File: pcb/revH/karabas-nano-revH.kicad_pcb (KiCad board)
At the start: 2 copper layers, 99.6 x 99.6 mm, 161 parts, among them J1 USB_B_Micro, J10 PWR, J11 AVR ISP, J2 TAPE IN/OUT, J3 A/V, J4 BUS, J5 KEYBOARD, J6 BUS, J7 JTAG, J9 RGB, Q2 BC856, SW1 RESET, SW10 8, SW11 9, SW12 0, SW13 Q, SW14 A, SW15 CS, SW16 W, SW17 S, SW18 Z, SW19 E, SW2 NMI, SW20 D, SW21 X, SW22 R, SW23 F, SW24 C, SW25 T, SW26 G, SW27 V, SW28 Y, SW29 H, SW3 1, SW30 B, SW31 U, SW32 J, SW33 N, SW34 I, SW35 K, SW36 M, SW37 O, SW38 L, SW39 SS, SW4 2, SW40 P, SW41 Enter, SW42 Space, SW5 3, SW6 4, SW7 5, SW8 6, SW9 7, U1 Z80, U13 LM1117-3.3, U2 39F040, U3 CY62167ELL, U4 ATmega8A-AU, U5 ESP-12E, U6 EPM3256ATC144, U7 MicroSD, U8 LM311, U9 AD724, Y1 28MHz, Y3 4.43MHz, Y4 20MHz

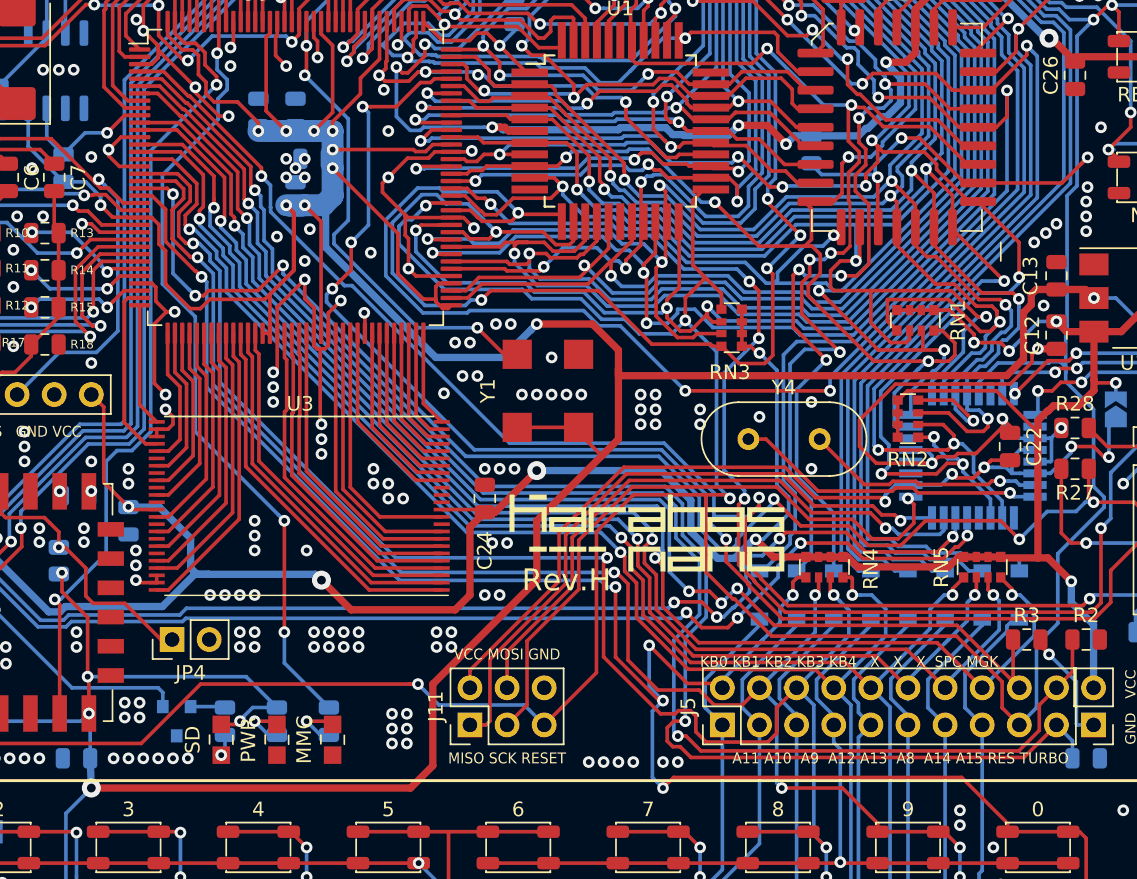
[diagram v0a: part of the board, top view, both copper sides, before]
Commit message: Added 3.3/5v selectors for memory and generator
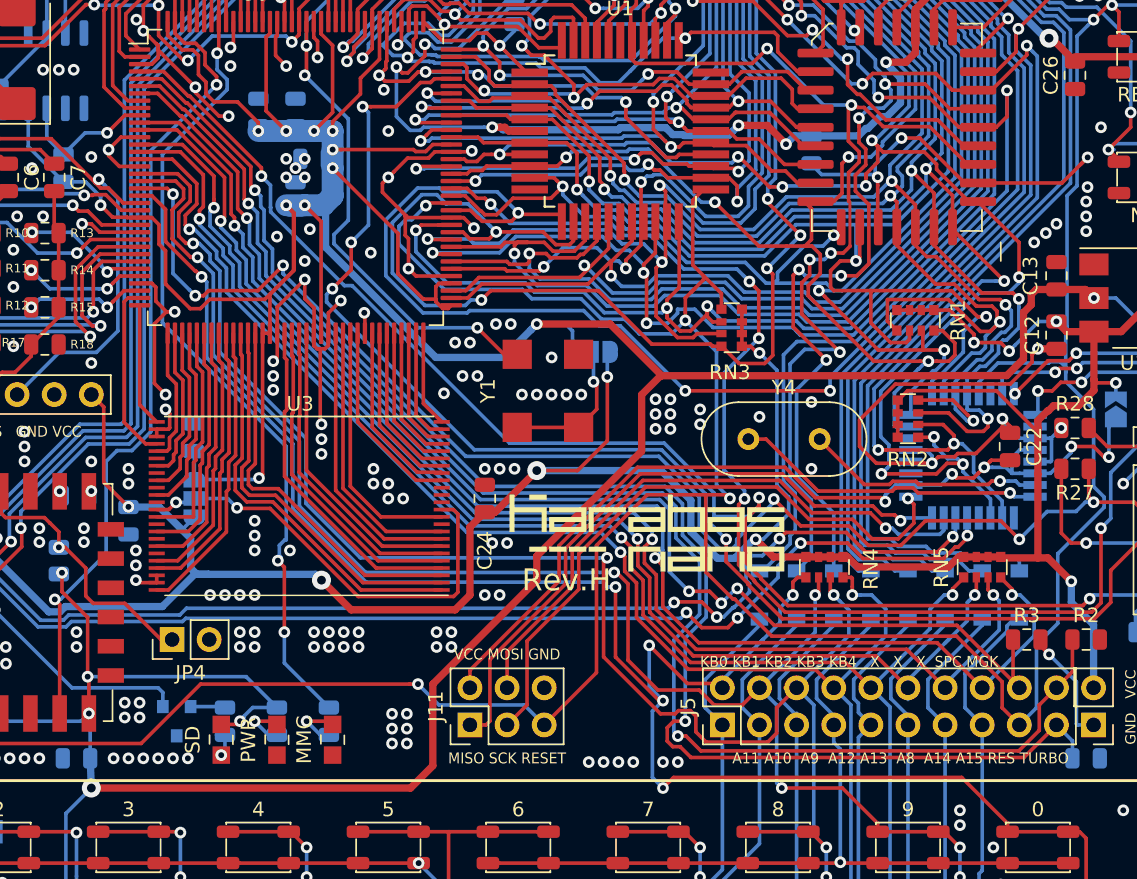
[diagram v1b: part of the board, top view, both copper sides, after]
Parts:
- removed the G*** at (144.5, 93.7)
- added C1: 100nF, Capacitor_SMD:C_0805_2012Metric, B.Cu at (118.7, 98.4)
- added JP5: 3/5V, Jumper:SolderJumper-3_P1.3mm_Open_RoundedPad1.0x1.5mm, B.Cu at (146.0, 92.6)
- added JP6: 3/5V, Jumper:SolderJumper-3_P1.3mm_Open_RoundedPad1.0x1.5mm, B.Cu at (118.8, 102.6)
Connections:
- U3 pad 12: VCC -> Net-(JP6-Pad2)
- U3 pad 37: VCC -> Net-(JP6-Pad2)
- Y1 pad 1: +3V3 -> Net-(JP5-Pad2)
- Y1 pad 4: +3V3 -> Net-(JP5-Pad2)
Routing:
- net Net-(JP6-Pad2): track 0.00 -> 30.4 mm, vias 0 -> 2
- net +3V3: track 356.2 -> 369.6 mm, vias 18 -> 19
- net Net-(JP5-Pad2): track 0.00 -> 10.4 mm, vias 0 -> 1
- net VCC: track 386.0 -> 394.5 mm, vias 20 -> 21
- net /MA15: track 26.2 -> 27.9 mm
- net /MA14: track 25.4 -> 27.2 mm
- net /MA13: track 24.6 -> 26.4 mm
- net KB2: track 223.4 -> 224.8 mm
- net KB1: track 247.4 -> 248.8 mm
- net KB0: track 281.9 -> 283.3 mm
- net GND: track 215.2 -> 214.3 mm, vias 366 -> 365
- net /MD4: track 14.7 -> 15.5 mm
- net /MAPCOND: track 75.6 -> 76.2 mm
- net /MD5: track 15.9 -> 16.5 mm
- net /VCCJP: track 64.1 -> 63.6 mm
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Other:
- board text added: "ESP Flash mode"
- board text added: "Generator 5V 3.3V"
- board text added: "Memory 5V 3.3V"

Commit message: small improvements
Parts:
- added G***: LOGO, footprints:karabas_nano_logo3-bmask, F.Cu at (185.5, 133.2)
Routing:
- net /D6: track 112.5 -> 113.5 mm
- net /A4: track 46.9 -> 46.3 mm
